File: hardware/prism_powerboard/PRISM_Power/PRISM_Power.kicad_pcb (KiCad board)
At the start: 2 copper layers, 46 parts, among them IC2 LP87564WRNFTQ1, J1 UJ32-21-C-H-G-HMT-LT-P24-TR, Q1 AO3400A, Q2 AO3400A, U1 STM32G031F6Px, U2 BQ25895RTW, U3 BQ297xy, U4 MAX17048G+T10

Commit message: Routing Updates
Added pads to the board, some more routing and trying to optimize
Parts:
- added 1V0: Pad, Library:SimpleSquarePad, F.Cu at (188.5, 108.7)
- added 1V35: Pad, Library:SimpleSquarePad, F.Cu at (188.5, 98.0)
- added 1V8: Pad, Library:SimpleSquarePad, F.Cu at (188.5, 73.5)
- added 2V1: Pad, Library:SimpleSquarePad, F.Cu at (188.5, 84.0)
- added C41: 100nF, Capacitor_SMD:C_01005_0402Metric, F.Cu at (159.2, 93.2)
- added C42: 100nF, Capacitor_SMD:C_0201_0603Metric, F.Cu at (160.3, 93.9)
- moved C4 45.9 mm to (126.3, 99.4)
- moved U3 45.9 mm to (133.7, 121.4)
- moved C1 45.9 mm to (130.8, 87.4)
- moved C14 45.9 mm to (148.8, 99.9)
- moved C15 45.9 mm to (153.3, 89.9)
- moved C16 45.9 mm to (153.8, 97.4)
- moved C18 45.9 mm to (176.8, 113.9)
- moved C19 45.9 mm to (176.8, 95.4)
- moved C2 45.9 mm to (136.3, 89.9)
- moved C20 45.9 mm to (180.3, 113.9)
- moved C3 45.9 mm to (128.8, 91.9)
- moved C43 45.9 mm to (180.3, 95.4)
- moved C45 45.9 mm to (180.3, 73.4)
- moved C6 45.9 mm to (149.8, 116.4)
- moved C7 45.9 mm to (141.3, 96.9)
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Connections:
- IC2 pad 15: EN2 -> EN2_PMIC
- IC2 pad 16: PGD_S -> PwrGoodSgnl
- IC2 pad 2: EN3 -> EN3_PMIC
- IC2 pad 7: EN1 -> EN1_PMIC
- U1 pad 12: INT_PMIC -> PwrGoodSgnl
- U1 pad 16: EN_PMIC -> EN1_PMIC
- U1 pad 2: unconnected-(U1-PB9/PC14-Pad2) -> EN3_PMIC
- U1 pad 3: unconnected-(U1-PC15-Pad3) -> EN2_PMIC
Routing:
- net EN2_PMIC: track 0.00 -> 55.9 mm, vias 0 -> 2
- net FB_B0: track 49.6 -> 82.4 mm
- net PwrGoodSgnl: track 0.00 -> 32.2 mm, vias 0 -> 2
- net FB_B2: track 45.9 -> 77.1 mm
- net FB_B1: track 34.4 -> 63.0 mm
- net EN1_PMIC: track 0.00 -> 23.5 mm, vias 0 -> 3
- net FB_B3: track 34.8 -> 57.4 mm
- net EN3_PMIC: track 0.00 -> 19.8 mm, vias 0 -> 4
- net SWDIO: track 18.8 -> 5.59 mm, vias 2 -> 3
- net SWCLK: track 18.9 -> 5.74 mm, vias 2 -> 3
- net SYS_3V5: track 93.9 -> 87.6 mm
- net SPI_MISO_1V8: track 0.00 -> 3.26 mm, vias 0 -> 1
- net SPI_MOSI_1V8: track 0.00 -> 2.96 mm, vias 0 -> 1
- net EN2: track 2.88 -> 0.00 mm, vias 1 -> 0
- net SPI_NSS_1V8: track 0.00 -> 2.51 mm, vias 0 -> 1
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
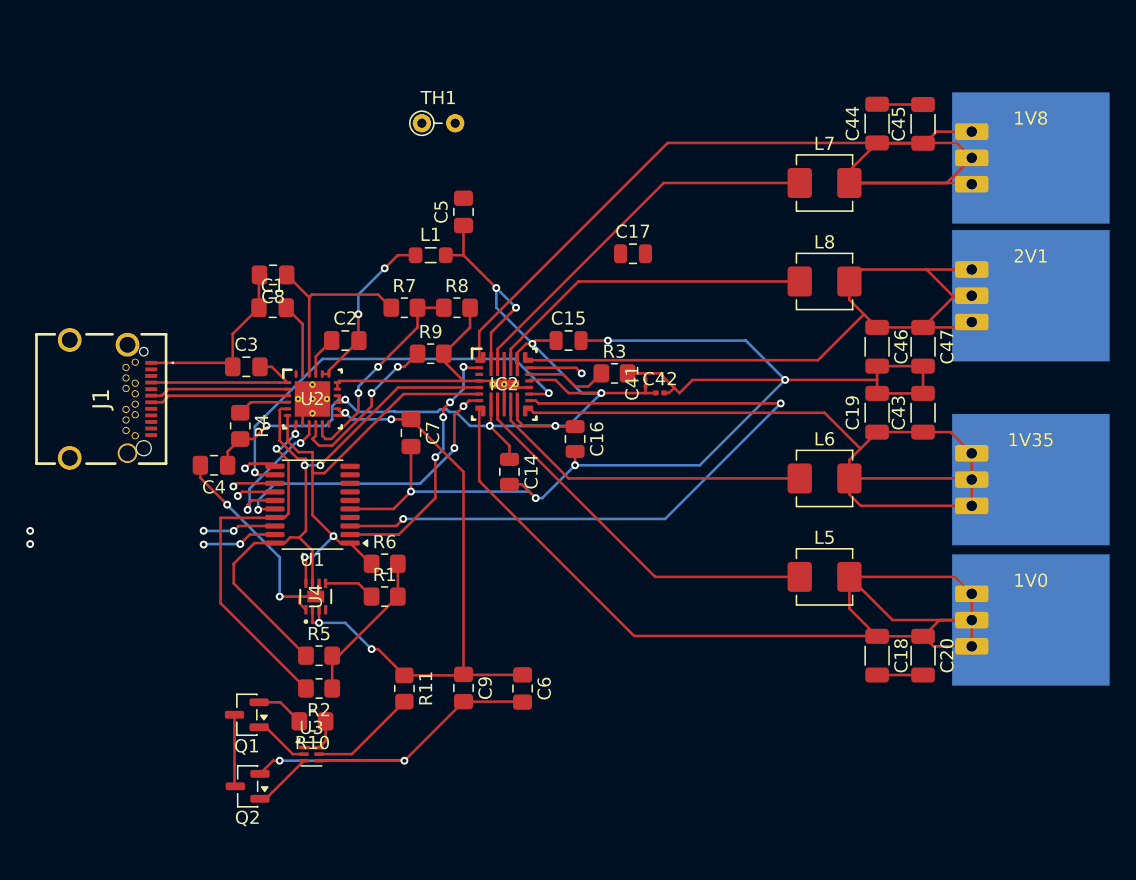
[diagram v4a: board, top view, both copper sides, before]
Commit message: Routing Updates
Added pads to everything. Need to add LDO on schematic and add to PCB. Almost done, may need to do impedance matching for SPI traces. Pads are all set and edge set.
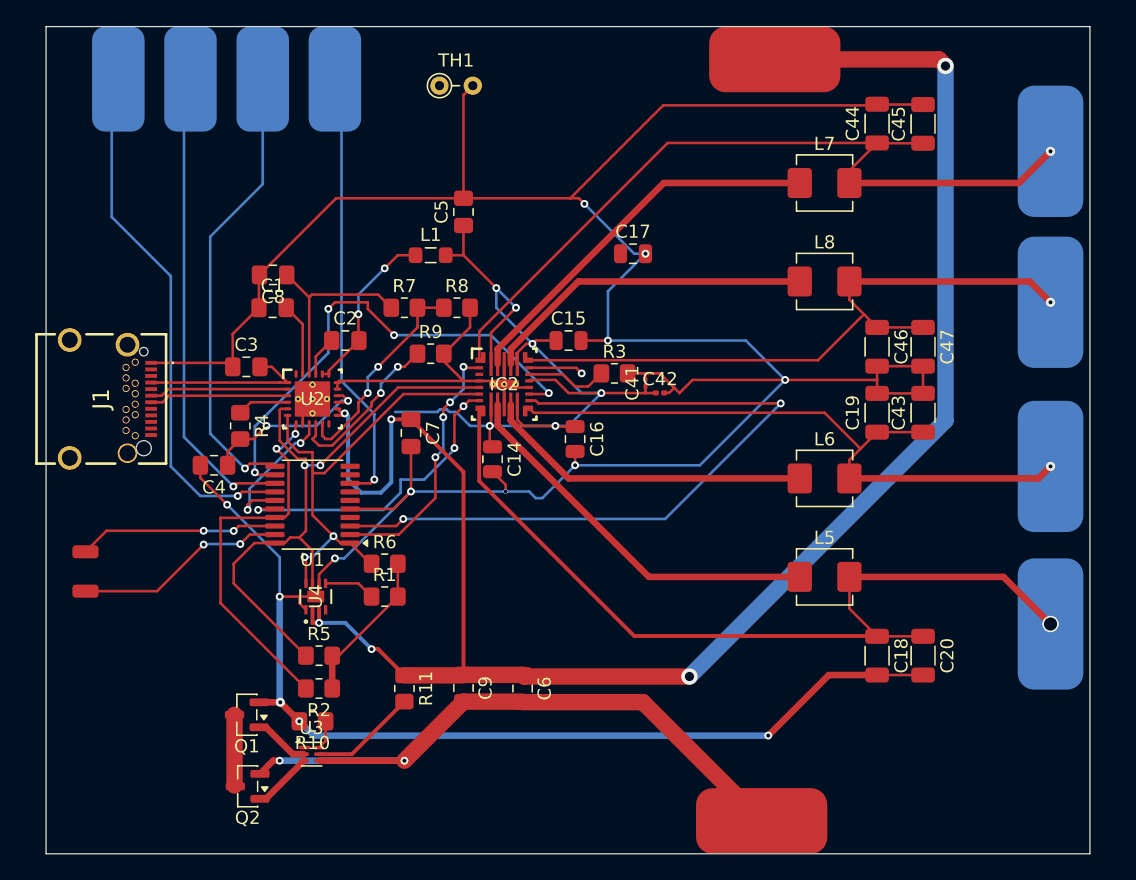
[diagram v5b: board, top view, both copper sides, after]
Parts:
- removed 1V0, 1V35, 1V8, 2V1: Pad, Library:SimpleSquarePad
- added ?: , , F.Cu at (124.5, 70.0)
- added ?: , , F.Cu at (168.0, 126.5)
- added ?: , , F.Cu at (135.5, 70.0)
- added ?: , , F.Cu at (130.0, 70.0)
- added ?: , , B.Cu at (169.0, 68.5)
- added REF**: SolderWirePad_1x01_SMD_1x2mm, Connector_Wire:SolderWirePad_1x01_SMD_1x2mm, F.Cu at (116.5, 106.0)
- added REF**: SolderWirePad_1x01_SMD_1x2mm, Connector_Wire:SolderWirePad_1x01_SMD_1x2mm, F.Cu at (116.5, 109.0)
- added REF**: SolderWirePad_1x01_SMD_5x10mm, Connector_Wire:SolderWirePad_1x01_SMD_5x10mm, B.Cu at (190.0, 87.0)
- added REF**: SolderWirePad_1x01_SMD_5x10mm, Connector_Wire:SolderWirePad_1x01_SMD_5x10mm, B.Cu at (190.0, 75.5)
- added REF**: SolderWirePad_1x01_SMD_4x8mm, Connector_Wire:SolderWirePad_1x01_SMD_4x8mm, B.Cu at (119.0, 70.0)
- added REF**: SolderWirePad_1x01_SMD_5x10mm, Connector_Wire:SolderWirePad_1x01_SMD_5x10mm, B.Cu at (190.0, 111.5)
- added REF**: SolderWirePad_1x01_SMD_5x10mm, Connector_Wire:SolderWirePad_1x01_SMD_5x10mm, B.Cu at (190.0, 99.5)
- moved TH1 3.16 mm to (143.5, 70.5)
- moved C14 1.61 mm to (147.5, 99.0)
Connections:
- IC2 pad 15: EN2_PMIC -> EN2
- IC2 pad 16: PwrGoodSgnl -> PGD_S
- IC2 pad 2: EN3_PMIC -> EN3
- IC2 pad 7: EN1_PMIC -> EN1
- U1 pad 12: PwrGoodSgnl -> INT_PMIC
- U1 pad 16: EN1_PMIC -> EN_PMIC
- U1 pad 2: EN3_PMIC -> unconnected-(U1-PB9/PC14-Pad2)
- U1 pad 3: EN2_PMIC -> unconnected-(U1-PC15-Pad3)
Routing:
- net GND: track 164.9 -> 305.7 mm, vias 7 -> 13
- net (no net): track 0.00 -> 137.4 mm, vias 0 -> 13
- net +BATT: track 47.4 -> 138.2 mm, vias 4 -> 6
- net EN2_PMIC: track 55.9 -> 0.00 mm, vias 2 -> 0
- net SPI_MOSI_1V8: track 2.96 -> 40.6 mm
- net SPI_SCK_1V8: track 0.00 -> 35.1 mm, vias 0 -> 1
- net SPI_MISO_1V8: track 3.26 -> 36.1 mm
- net SPI_NSS_1V8: track 2.51 -> 34.9 mm
- net PwrGoodSgnl: track 32.2 -> 0.00 mm, vias 2 -> 0
- net EN1_PMIC: track 23.5 -> 0.00 mm, vias 3 -> 0
- net -BATT: track 28.8 -> 50.8 mm
- net EN3_PMIC: track 19.8 -> 0.00 mm, vias 4 -> 0
- net FB_B0: track 82.4 -> 66.5 mm, vias 0 -> 1
- net FB_B2: track 77.1 -> 62.3 mm, vias 0 -> 1
- net FB_B1: track 63.0 -> 50.1 mm, vias 0 -> 1
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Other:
- board outline added: 79.5 x 63 mm

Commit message: DRC Required
Everything should be done, just reviewing DRC and making sure everything looks good. Quite a few errors, few seem to be relevant or real.
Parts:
- added REF**: SolderWirePad_1x01_SMD_3x6mm, Connector_Wire:SolderWirePad_1x01_SMD_3x6mm, F.Cu at (135.0, 127.5)
- added REF**: SolderWirePad_1x01_SMD_3x6mm, Connector_Wire:SolderWirePad_1x01_SMD_3x6mm, B.Cu at (135.0, 127.5)
- added U5: AMS1117-1.8, Package_TO_SOT_SMD:SOT-223-3_TabPin2, F.Cu at (145.5, 108.7)
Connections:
- IC2 pad 27: (no net) -> GND
- IC2 pad V: (no net) -> GND
- U1 pad 12: INT_PMIC -> PGD_S
- U1 pad 16: EN_PMIC -> EN1
- U1 pad 2: unconnected-(U1-PB9/PC14-Pad2) -> EN3
- U1 pad 3: unconnected-(U1-PC15-Pad3) -> EN2
- U1 pad 4: +1V8_LDO -> Net-(U1-VDD)
- U2 pad 12: NC -> (no net)
- U2 pad 24: NC -> (no net)
- U2 pad V: (no net) -> GND
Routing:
- net (no net): track 137.4 -> 0.00 mm, vias 13 -> 0
- net EN2: track 0.00 -> 55.4 mm, vias 0 -> 2
- net PGD_S: track 0.00 -> 38.1 mm, vias 0 -> 4
- net NRST: track 0.00 -> 31.4 mm, vias 0 -> 2
- net EN1: track 0.00 -> 23.4 mm, vias 0 -> 3
- net EN3: track 0.00 -> 20.6 mm, vias 0 -> 4
- net Net-(U2-TS): track 16.4 -> 33.5 mm, vias 2 -> 3
- net Net-(U1-VDD): track 0.00 -> 11.3 mm, vias 0 -> 2
- net GND: track 305.7 -> 298.7 mm, vias 13 -> 14
- net -BATT: track 50.8 -> 57.2 mm, vias 2 -> 4
- net +BATT: track 138.2 -> 142.9 mm

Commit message: Powerboard SOM
The Powerboard System-on-Module is finished. Quite a few errors, none of them actually important or cause issues, simply naming or meshing issues. Board prototype has been sent to manufacture. May update in the future for common module connector.
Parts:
- gave numbers to parts that had none: 3
- renumbered REF** to MOSI_1V8
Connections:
- J1 pad B1: unconnected-(J1-GND_3-PadB1) -> GND
- J1 pad B12: unconnected-(J1-GND_4-PadB12) -> GND
- J1 pad B4: unconnected-(J1-VBUS_3-PadB4) -> USB_VCC
- J1 pad B9: unconnected-(J1-VBUS_4-PadB9) -> USB_VCC
- U1 pad 7: unconnected-(U1-PA0-Pad7) -> PMIC_RST
- U5 pad 1: -BATT -> GND
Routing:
- net GND: track 298.7 -> 274.8 mm, vias 14 -> 15
- net USB_VCC: track 13.0 -> 26.1 mm, vias 0 -> 3
- net FB_B1: track 50.1 -> 60.9 mm
- net FB_B3: track 50.8 -> 61.3 mm
- net FB_B0: track 66.5 -> 76.7 mm
- net FB_B2: track 62.3 -> 72.2 mm
- net SYS_3V5: track 81.9 -> 90.8 mm, vias 8 -> 10
- net -BATT: track 57.2 -> 51.2 mm, vias 4 -> 2
- net PMIC_RST: track 4.18 -> 8.79 mm, vias 1 -> 2
- net EN1: vias 3 -> 2
- added copper zone on B.Cu, net GND
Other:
- board size 79.5 x 63 mm -> 79.5 x 64 mm
